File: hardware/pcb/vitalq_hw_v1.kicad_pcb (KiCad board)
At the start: 4 copper layers, 36.5 x 32 mm, 146 parts, among them J1 USB-C, J2 LiPo pads, J3 FSR pads, J5 ECG pads, J6 EDA pads, Q1 CSD13380F3, U1 ESP32-WROOM-32E-N8R2, U10 AS7341-DLGM, U11 TMP117AIDRVR, U12 MLX90632SLD-DCB-100-SP, U13 BME280, U14 LSM6DSV80XTR, U15 TPS61240YFFR, U16 SFH 7072, U17 MAX17048G+T10, U18 W25Q512JVEIQ, U19 TCA6408ARSVR, U2 MCP73831T-2ACI/OT, U20 TMP117AIDRVR, U3 TPS63802DLAR, U4 TPS7A2018PDBVR, U5 CP2102N-A02-GQFN28R, U6 AFE4900YZR, U7 AD5940BCBZ-RL7, U8 ADS1292RIRSMT, U9 PCA9306DCUR

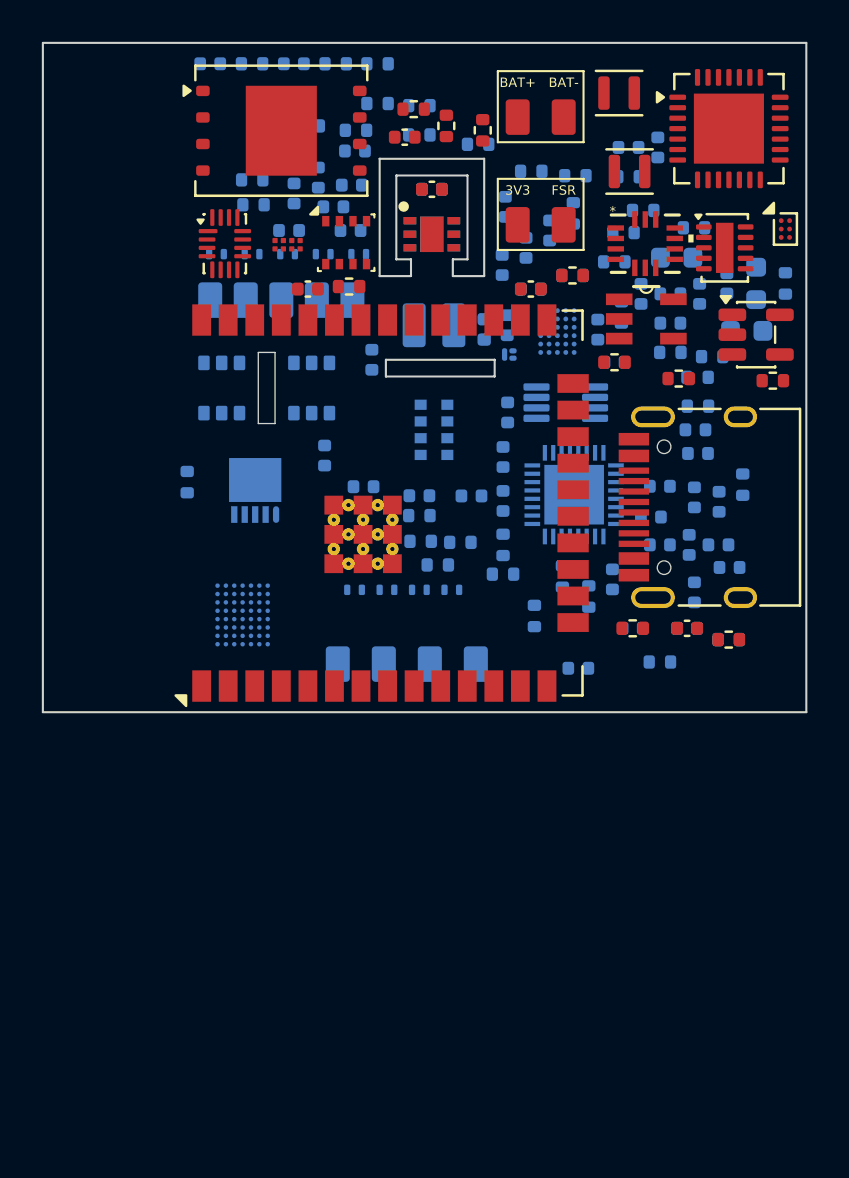
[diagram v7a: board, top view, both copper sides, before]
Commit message: Add defibrillator clamps and a charge-temperature cut-off.
Series electrode resistors are now DPCR2512 51k pulse parts, with an S30-A90X gas discharge tube on each patient pad ahead of the existing TPD1E10B06. The MCP73831 stays; a PicoStar FET floats PROG until firmware enables charge, and a 3-pin cell pad feeds a 10k NTC into GPIO39.

Co-authored-by: Riyu-D1 <Riyu-D1@users.noreply.github.com>
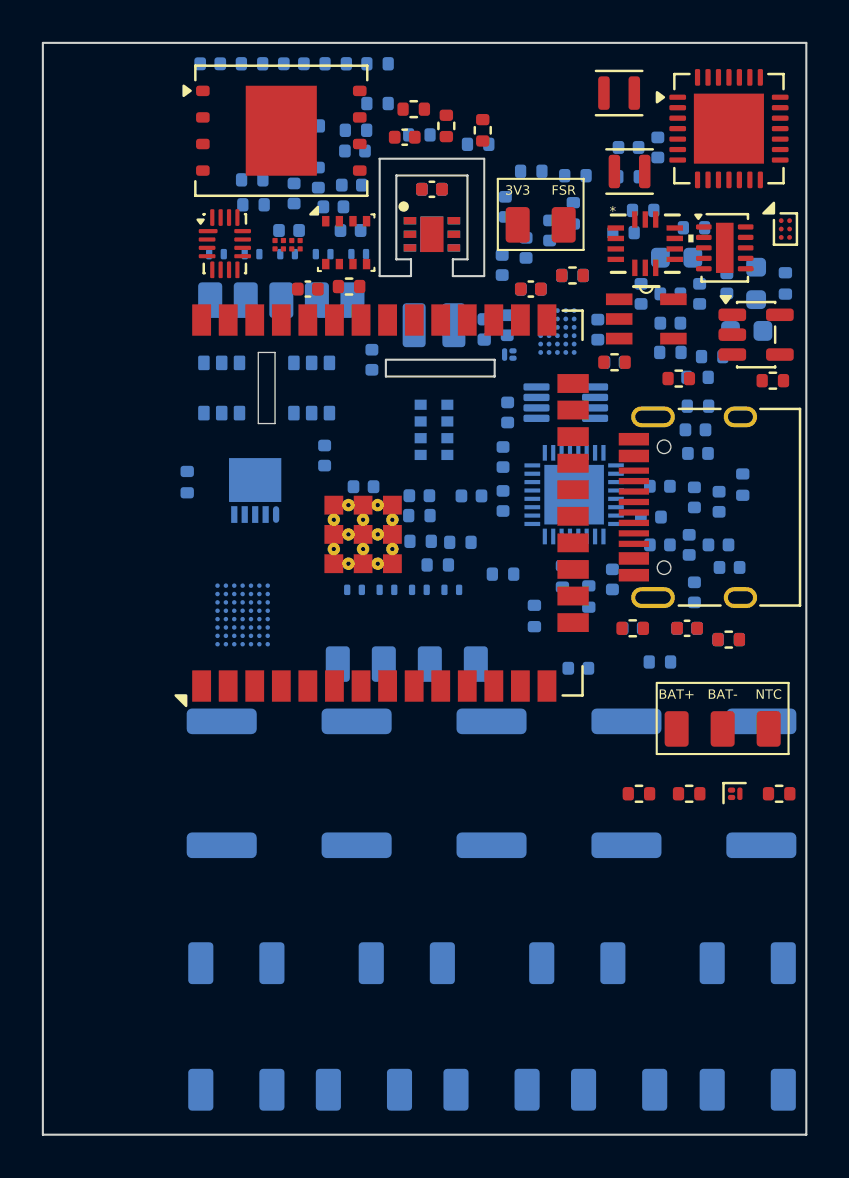
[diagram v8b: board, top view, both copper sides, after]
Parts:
- added D12: S30-A90X, vitalq:GDT_S30, B.Cu at (9.25, 50.0)
- added D13: S30-A90X, vitalq:GDT_S30, B.Cu at (15.3, 50.0)
- added D14: S30-A90X, vitalq:GDT_S30, B.Cu at (21.4, 50.0)
- added D15: S30-A90X, vitalq:GDT_S30, B.Cu at (27.6, 50.0)
- added D16: S30-A90X, vitalq:GDT_S30, B.Cu at (33.7, 50.0)
- added D17: S30-A90X, vitalq:GDT_S30, B.Cu at (9.25, 44.0)
- added D18: S30-A90X, vitalq:GDT_S30, B.Cu at (17.4, 44.0)
- added D19: S30-A90X, vitalq:GDT_S30, B.Cu at (25.6, 44.0)
- added D20: S30-A90X, vitalq:GDT_S30, B.Cu at (33.7, 44.0)
- added Q2: CSD13380F3, Package_DFN_QFN:Texas_PicoStar_DFN-3_0.69x0.60mm, F.Cu at (33.1, 35.9)
- added R59: 100k, Resistor_SMD:R_0402_1005Metric, F.Cu at (35.2, 35.9)
- added R60: 10k, Resistor_SMD:R_0402_1005Metric, F.Cu at (30.9, 35.9)
- added R61: 10k, Resistor_SMD:R_0402_1005Metric, F.Cu at (28.5, 35.9)
- R32, R33, R34, R35, R36: value 49.9k -> 51k; footprint Resistor_SMD:R_0402_1005Metric -> Resistor_SMD:R_2512_6332Metric
- moved R34 32.6 mm to (21.4, 35.4), turned to 90 degrees
- moved R32 31.2 mm to (8.55, 35.4), turned to 90 degrees
- moved R33 30.6 mm to (15.0, 35.4), turned to 90 degrees
- moved J2 30.5 mm to (32.5, 32.8)
- moved R36 23.5 mm to (34.4, 35.4)
- moved R35 12.8 mm to (27.9, 35.4)
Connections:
- D1 pad 1: ECG1_PAD -> ECG_P
- D2 pad 1: ECG2_PAD -> ECG_N
- D3 pad 1: RLD_PAD -> RLDOUT
- D4 pad 1: AFE_P_PAD -> AFE_P_AC
- D5 pad 1: AFE_N_PAD -> AFE_N_AC
- D6 pad 1: EDA_CE_PAD -> CE_ISO
- D7 pad 1: EDA_SE_PAD -> SE_ISO
- D8 pad 1: EDA_RE_PAD -> RE0
- D9 pad 1: EDA_DE_PAD -> DE0
- R3 pad 2: GND -> PROG_RTN
- U1 pad 5: unconnected-(U1-SENSOR_VN-Pad5) -> NTC_ADC
- U19 pad 10: unconnected-(U19-P7-Pad10) -> CHG_EN
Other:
- board size 36.5 x 32 mm -> 36.5 x 52.2 mm
